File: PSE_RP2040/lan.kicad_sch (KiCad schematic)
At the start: 32 parts

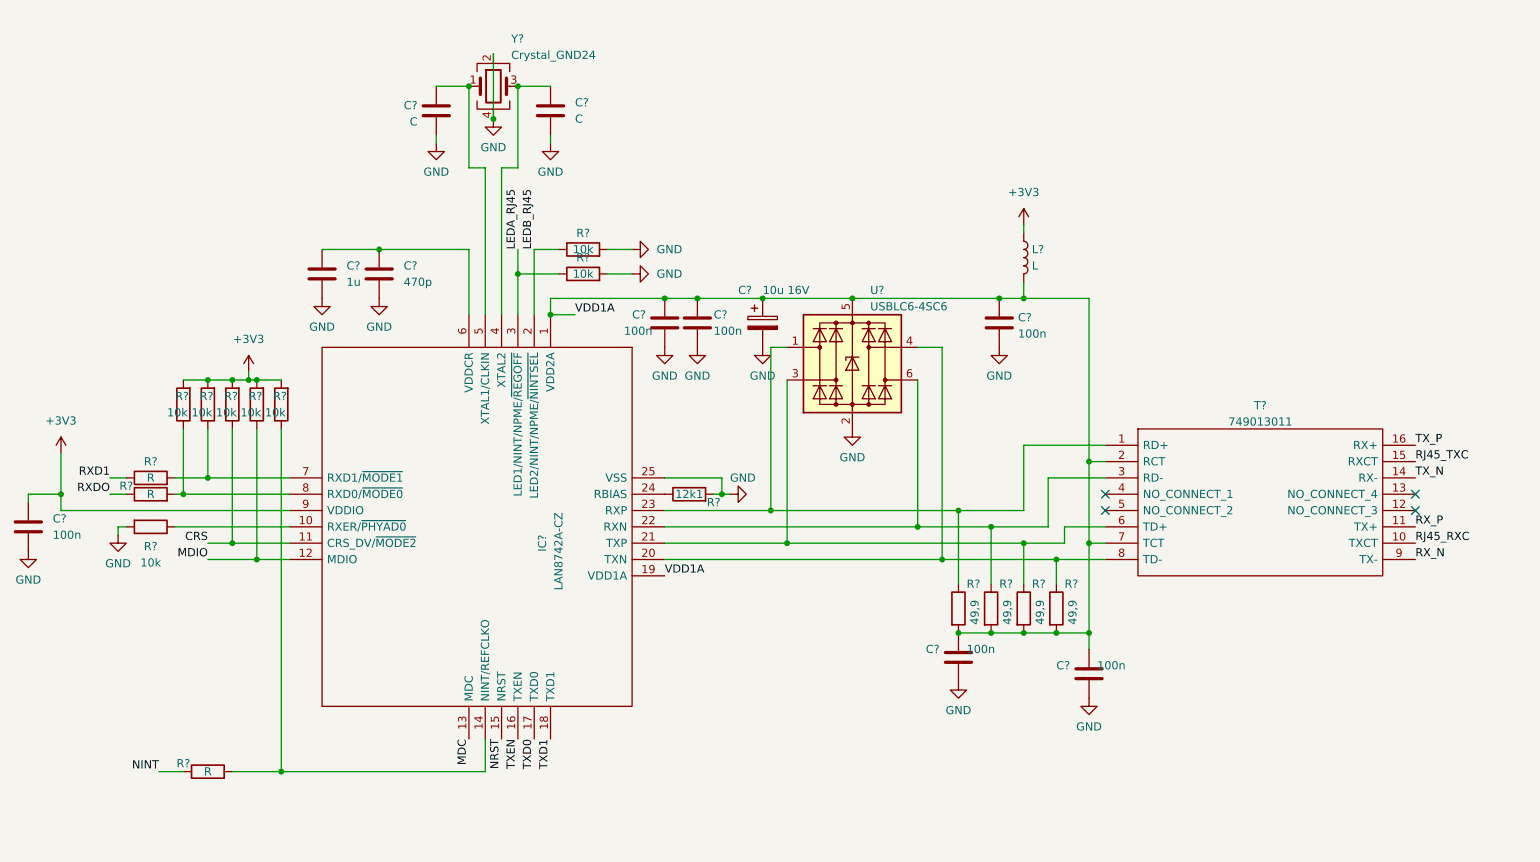
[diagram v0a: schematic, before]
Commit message: aggiornamento schematico
etichette globali, testpoint, assegnamento footprint (ne mancano ancora)
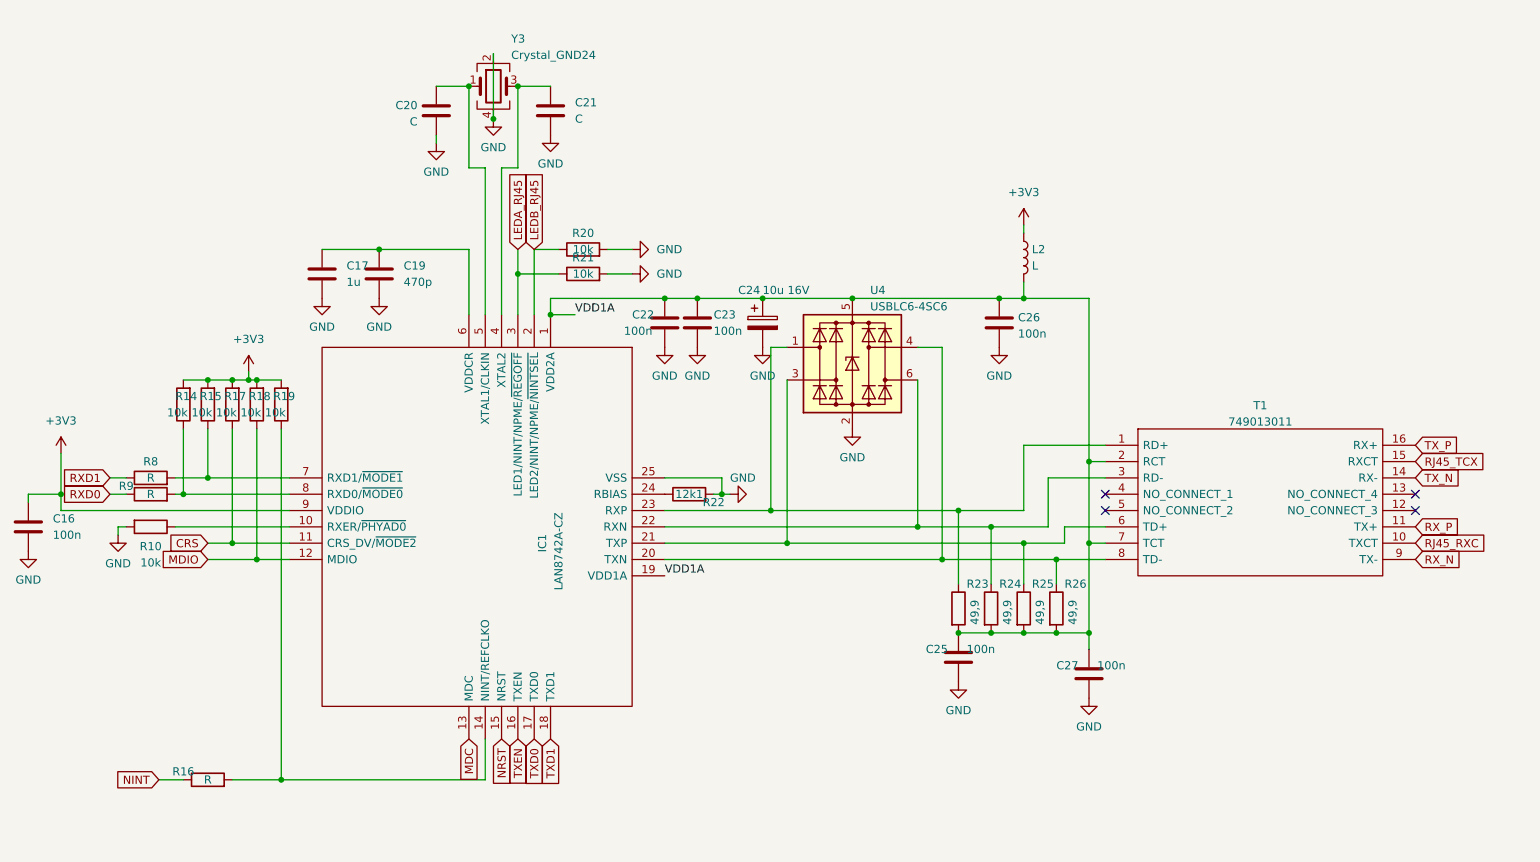
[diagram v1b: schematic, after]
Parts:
- IC1: renamed from IC?; footprint QFN50P400X400X100-25N-D -> (none)
- T1: renamed from T?; footprint 749013011 -> (none)
- gave numbers to parts that had none: 30
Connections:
- net RJ45_TXC renamed RJ45_TCX
- net RXDO renamed RXD0
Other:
- moved on the sheet: R16

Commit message: assegnamento footprint PAM7Q
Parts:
- C16, C17, C19, C22, C23, C25, C26, C27: footprint (none) -> Capacitor_SMD:C_0603_1608Metric
- C24: footprint (none) -> Capacitor_SMD:C_0805_2012Metric
- L2: footprint (none) -> Inductor_SMD:L_0603_1608Metric
- R10, R14, R15, R16, R17, R18, R19, R20, R21, R22, R23, R24, R25, R26, R8, R9: footprint (none) -> Resistor_SMD:R_0603_1608Metric
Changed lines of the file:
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@@
     (property "Reference" "R16" (id 0) (at 43.18 133.35 90))
     (property "Value" "R" (id 1) (at 46.99 134.62 90))
-    (property "Footprint" "" (id 2) (at 46.99 136.398 90)
+    (property "Footprint" "Resistor_SMD:R_0603_1608Metric" (id 2) (at 46.99 136.398 90)
       (effects (font (size 1.27 1.27)) hide)
     )
@@
       (effects (font (size 1.27 1.27)) (justify right))
     )
-    (property "Footprint" "" (id 2) (at 56.388 76.2 90)
+    (property "Footprint" "Resistor_SMD:R_0603_1608Metric" (id 2) (at 56.388 76.2 90)
       (effects (font (size 1.27 1.27)) hide)
     )
@@
     (property "Reference" "R9" (id 0) (at 34.29 88.9 90))
     (property "Value" "R" (id 1) (at 38.1 90.17 90))
-    (property "Footprint" "" (id 2) (at 38.1 91.948 90)
+    (property "Footprint" "Resistor_SMD:R_0603_1608Metric" (id 2) (at 38.1 91.948 90)
       (effects (font (size 1.27 1.27)) hide)
     )
@@
       (effects (font (size 1.27 1.27)) (justify left))
     )
-    (property "Footprint" "" (id 2) (at 65.7352 59.69 0)
+    (property "Footprint" "Capacitor_SMD:C_0603_1608Metric" (id 2) (at 65.7352 59.69 0)
       (effects (font (size 1.27 1.27)) hide)
     )
@@
       (effects (font (size 1.27 1.27)) (justify left))
     )
-    (property "Footprint" "" (id 2) (at 167.132 107.95 90)
+    (property "Footprint" "Resistor_SMD:R_0603_1608Metric" (id 2) (at 167.132 107.95 90)
       (effects (font (size 1.27 1.27)) hide)
     )
@@
       (effects (font (size 1.27 1.27)) (justify left))
     )
-    (property "Footprint" "" (id 2) (at 172.212 107.95 90)
+    (property "Footprint" "Resistor_SMD:R_0603_1608Metric" (id 2) (at 172.212 107.95 90)
       (effects (font (size 1.27 1.27)) hide)
     )
@@
     (property "Reference" "R10" (id 0) (at 38.1 98.2964 90))
     (property "Value" "10k" (id 1) (at 38.1 100.8333 90))
-    (property "Footprint" "" (id 2) (at 38.1 93.472 90)
+    (property "Footprint" "Resistor_SMD:R_0603_1608Metric" (id 2) (at 38.1 93.472 90)
       (effects (font (size 1.27 1.27)) hide)
     )
@@
       (effects (font (size 1.27 1.27)) (justify right))
     )
-    (property "Footprint" "" (id 2) (at 44.958 76.2 90)
+    (property "Footprint" "Resistor_SMD:R_0603_1608Metric" (id 2) (at 44.958 76.2 90)
       (effects (font (size 1.27 1.27)) hide)
     )
@@
     (property "Reference" "R21" (id 0) (at 105.41 53.34 90))
     (property "Value" "10k" (id 1) (at 105.41 55.88 90))
-    (property "Footprint" "" (id 2) (at 105.41 57.658 90)
+    (property "Footprint" "Resistor_SMD:R_0603_1608Metric" (id 2) (at 105.41 57.658 90)
       (effects (font (size 1.27 1.27)) hide)
     )
@@
       (effects (font (size 1.27 1.27)) (justify left))
     )
-    (property "Footprint" "" (id 2) (at 134.3152 67.31 0)
+    (property "Footprint" "Capacitor_SMD:C_0805_2012Metric" (id 2) (at 134.3152 67.31 0)
       (effects (font (size 1.27 1.27)) hide)
     )
@@
       (effects (font (size 1.27 1.27)) (justify left))
     )
-    (property "Footprint" "" (id 2) (at 173.99 53.34 0)
+    (property "Footprint" "Inductor_SMD:L_0603_1608Metric" (id 2) (at 173.99 53.34 0)
       (effects (font (size 1.27 1.27)) hide)
     )
@@
       (effects (font (size 1.27 1.27)) (justify left))
     )
-    (property "Footprint" "" (id 2) (at 177.292 107.95 90)
+    (property "Footprint" "Resistor_SMD:R_0603_1608Metric" (id 2) (at 177.292 107.95 90)
       (effects (font (size 1.27 1.27)) hide)
     )
@@
       (effects (font (size 1.27 1.27)) (justify left))
     )
-    (property "Footprint" "" (id 2) (at 74.6252 59.69 0)
+    (property "Footprint" "Capacitor_SMD:C_0603_1608Metric" (id 2) (at 74.6252 59.69 0)
       (effects (font (size 1.27 1.27)) hide)
     )
@@
     (property "Reference" "R22" (id 0) (at 125.73 91.44 90))
     (property "Value" "12k1" (id 1) (at 121.92 90.17 90))
-    (property "Footprint" "" (id 2) (at 121.92 91.948 90)
+    (property "Footprint" "Resistor_SMD:R_0603_1608Metric" (id 2) (at 121.92 91.948 90)
       (effects (font (size 1.27 1.27)) hide)
     )
@@
       (effects (font (size 1.27 1.27)) (justify right))
     )
-    (property "Footprint" "" (id 2) (at 60.198 76.2 90)
+    (property "Footprint" "Resistor_SMD:R_0603_1608Metric" (id 2) (at 60.198 76.2 90)
       (effects (font (size 1.27 1.27)) hide)
     )
@@
       (effects (font (size 1.27 1.27)) (justify right))
     )
-    (property "Footprint" "" (id 2) (at 48.768 76.2 90)
+    (property "Footprint" "Resistor_SMD:R_0603_1608Metric" (id 2) (at 48.768 76.2 90)
       (effects (font (size 1.27 1.27)) hide)
     )
@@
       (effects (font (size 1.27 1.27)) (justify left))
     )
-    (property "Footprint" "" (id 2) (at 162.052 107.95 90)
+    (property "Footprint" "Resistor_SMD:R_0603_1608Metric" (id 2) (at 162.052 107.95 90)
       (effects (font (size 1.27 1.27)) hide)
     )
@@
       (effects (font (size 1.27 1.27)) (justify left))
     )
-    (property "Footprint" "" (id 2) (at 164.7952 119.38 0)
+    (property "Footprint" "Capacitor_SMD:C_0603_1608Metric" (id 2) (at 164.7952 119.38 0)
       (effects (font (size 1.27 1.27)) hide)
     )
@@
       (effects (font (size 1.27 1.27)) (justify right))
     )
-    (property "Footprint" "" (id 2) (at 52.578 76.2 90)
+    (property "Footprint" "Resistor_SMD:R_0603_1608Metric" (id 2) (at 52.578 76.2 90)
       (effects (font (size 1.27 1.27)) hide)
     )
@@
       (effects (font (size 1.27 1.27)) (justify left))
     )
-    (property "Footprint" "" (id 2) (at 185.1152 121.92 0)
+    (property "Footprint" "Capacitor_SMD:C_0603_1608Metric" (id 2) (at 185.1152 121.92 0)
       (effects (font (size 1.27 1.27)) hide)
     )
@@
     (property "Reference" "R20" (id 0) (at 105.41 49.53 90))
     (property "Value" "10k" (id 1) (at 105.41 52.07 90))
-    (property "Footprint" "" (id 2) (at 105.41 53.848 90)
+    (property "Footprint" "Resistor_SMD:R_0603_1608Metric" (id 2) (at 105.41 53.848 90)
       (effects (font (size 1.27 1.27)) hide)
     )
@@
       (effects (font (size 1.27 1.27)) (justify left))
     )
-    (property "Footprint" "" (id 2) (at 171.1452 67.31 0)
+    (property "Footprint" "Capacitor_SMD:C_0603_1608Metric" (id 2) (at 171.1452 67.31 0)
       (effects (font (size 1.27 1.27)) hide)
     )
@@
       (effects (font (size 1.27 1.27)) (justify left))
     )
-    (property "Footprint" "" (id 2) (at 20.0152 99.06 0)
+    (property "Footprint" "Capacitor_SMD:C_0603_1608Metric" (id 2) (at 20.0152 99.06 0)
       (effects (font (size 1.27 1.27)) hide)
     )
@@
     (property "Reference" "R8" (id 0) (at 38.1 85.09 90))
     (property "Value" "R" (id 1) (at 38.1 87.63 90))
-    (property "Footprint" "" (id 2) (at 38.1 89.408 90)
+    (property "Footprint" "Resistor_SMD:R_0603_1608Metric" (id 2) (at 38.1 89.408 90)
       (effects (font (size 1.27 1.27)) hide)
     )
@@
       (effects (font (size 1.27 1.27)) (justify left))
     )
-    (property "Footprint" "" (id 2) (at 119.0752 67.31 0)
+    (property "Footprint" "Capacitor_SMD:C_0603_1608Metric" (id 2) (at 119.0752 67.31 0)
       (effects (font (size 1.27 1.27)) hide)
     )
@@
       (effects (font (size 1.27 1.27)) (justify left))
     )
-    (property "Footprint" "" (id 2) (at 124.1552 67.31 0)
-      (effects (font (size 1.27 1.27)) hide)
-    )
+    (property "Footprint" "Capacitor_SMD:C_0603_1608Metric" (id 2) (at 124.1552 67.31 0)
+      (effects (font (size 1.27 1.27)) hide)
+    )

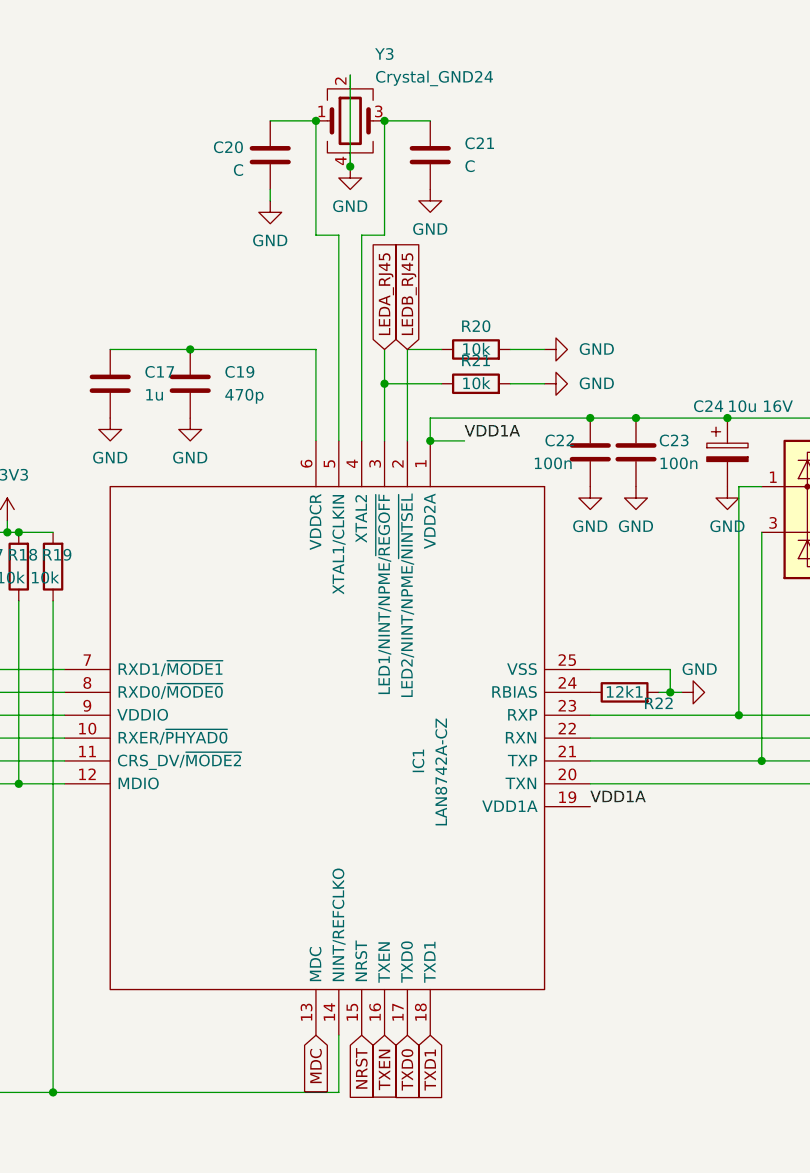
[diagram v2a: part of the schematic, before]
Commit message: footprint, aggiunto bottone rst
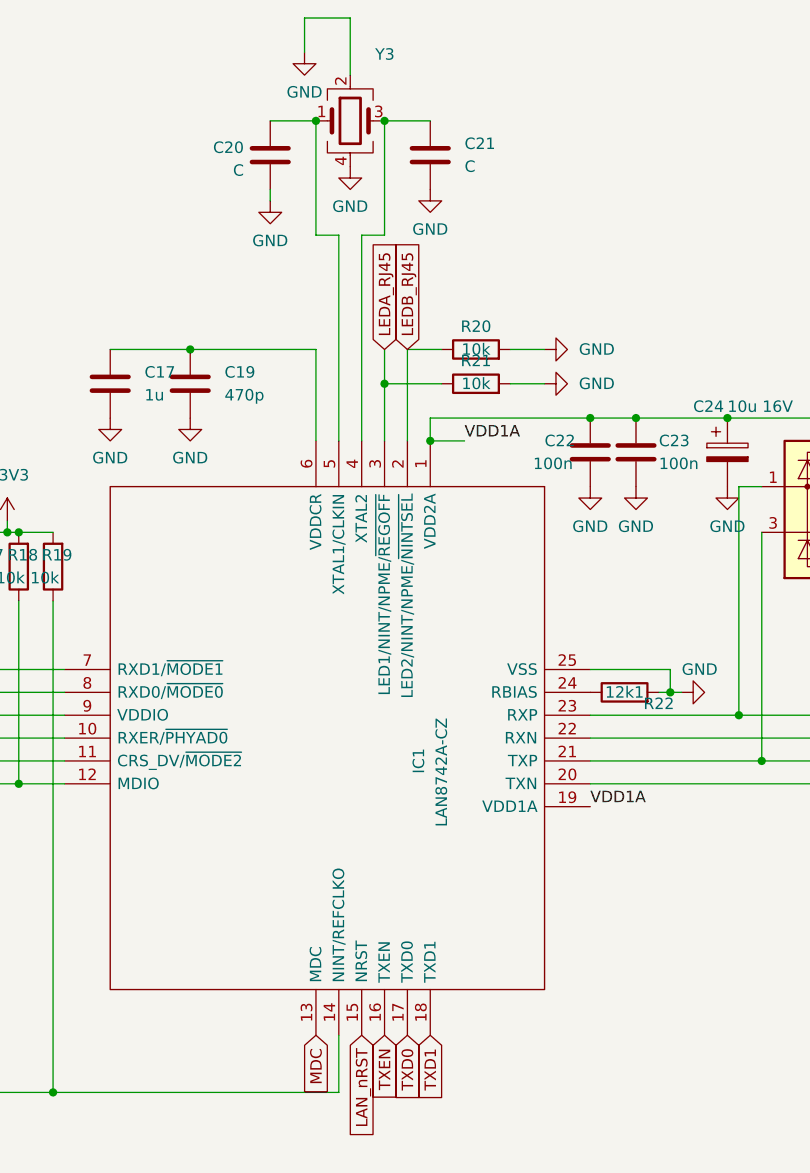
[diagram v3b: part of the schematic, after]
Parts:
- T1: footprint (none) -> Transformer_SMD:Transformer_Ethernet_Wuerth_749013011A
- Y3: value Crystal_GND24 -> (none)
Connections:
- net NRST renamed LAN_nRST
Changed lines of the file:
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@@
   (junction (at 50.8 97.79) (diameter 0) (color 0 0 0 0)
-  )
-  (junction (at 91.44 31.75) (diameter 0) (color 0 0 0 0)
   )
   (junction (at 127 90.17) (diameter 0) (color 0 0 0 0)
@@
     (stroke (width 0) (type default) (color 0 0 0 0))
   )
+  (wire (pts (xy 86.36 15.24) (xy 91.44 15.24))
+    (stroke (width 0) (type default) (color 0 0 0 0))
+  )
   (wire (pts (xy 24.13 90.17) (xy 24.13 83.82))
     (stroke (width 0) (type default) (color 0 0 0 0))
@@
     (stroke (width 0) (type default) (color 0 0 0 0))
   )
+  (wire (pts (xy 91.44 15.24) (xy 91.44 21.59))
+    (stroke (width 0) (type default) (color 0 0 0 0))
+  )
   (wire (pts (xy 50.8 80.01) (xy 50.8 97.79))
     (stroke (width 0) (type default) (color 0 0 0 0))
@@
     (stroke (width 0) (type default) (color 0 0 0 0))
   )
-  (wire (pts (xy 91.44 21.59) (xy 91.44 31.75))
-    (stroke (width 0) (type default) (color 0 0 0 0))
-  )
   (wire (pts (xy 184.15 59.69) (xy 184.15 85.09))
     (stroke (width 0) (type default) (color 0 0 0 0))
@@
   )
   (wire (pts (xy 24.13 90.17) (xy 19.05 90.17))
+    (stroke (width 0) (type default) (color 0 0 0 0))
+  )
+  (wire (pts (xy 86.36 19.05) (xy 86.36 15.24))
     (stroke (width 0) (type default) (color 0 0 0 0))
   )
@@
     )
   )
-  (global_label "NRST" (shape input) (at 92.71 128.27 270) (fields_autoplaced)
+  (global_label "LAN_nRST" (shape input) (at 92.71 128.27 270) (fields_autoplaced)
     (effects (font (size 1.27 1.27)) (justify right))
-    (property "Intersheet References" "${INTERSHEET_REFS}" (id 0) (at 92.7894 135.3718 90)
+    (property "Intersheet References" "${INTERSHEET_REFS}" (id 0) (at 92.6306 139.6052 90)
       (effects (font (size 1.27 1.27)) (justify right) hide)
     )
@@
     (property "Reference" "T1" (id 0) (at 210.82 76.361 0))
     (property "Value" "749013011" (id 1) (at 210.82 78.8979 0))
-    (property "Footprint" "" (id 2) (at 231.14 80.01 0)
+    (property "Footprint" "Transformer_SMD:Transformer_Ethernet_Wuerth_749013011A" (id 2) (at 231.14 80.01 0)
       (effects (font (size 1.27 1.27)) (justify left) hide)
     )
@@
     (pin "6")
   )
+  (symbol (lib_id "power:GND") (at 86.36 19.05 0) (unit 1)
+    (in_bom yes) (on_board yes) (fields_autoplaced)
+    (property "Reference" "#PWR0192" (id 0) (at 86.36 25.4 0)
+      (effects (font (size 1.27 1.27)) hide)
+    )
+    (property "Value" "GND" (id 1) (at 86.36 23.4934 0))
+    (property "Footprint" "" (id 2) (at 86.36 19.05 0)
+      (effects (font (size 1.27 1.27)) hide)
+    )
+    (property "Datasheet" "" (id 3) (at 86.36 19.05 0)
+      (effects (font (size 1.27 1.27)) hide)
+    )
+    (pin "1")
+  )
   (symbol (lib_id "Device:R") (at 46.99 76.2 180) (unit 1)
     (in_bom yes) (on_board yes) (fields_autoplaced)
@@
       (effects (font (size 1.27 1.27)) (justify left))
     )
-    (property "Value" "Crystal_GND24" (id 1) (at 94.2087 21.8241 0)
-      (effects (font (size 1.27 1.27)) (justify left))
-    )
+    (property "Value" "" (id 1) (at 94.2087 21.8241 0)
+      (effects (font (size 1.27 1.27)) (justify left))
+    )
